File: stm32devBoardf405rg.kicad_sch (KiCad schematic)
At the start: 54 parts, among them J1 Screw_Terminal_01x02, J2 SWD, J3 Conn_01x04, J4 Conn_01x04, J5 USB_B_Micro, Q1 AO3401A, SW1 SW_SPDT, U1 STM32F405RGT6, U2 USBLC6-2SC6, Y1 16MZ

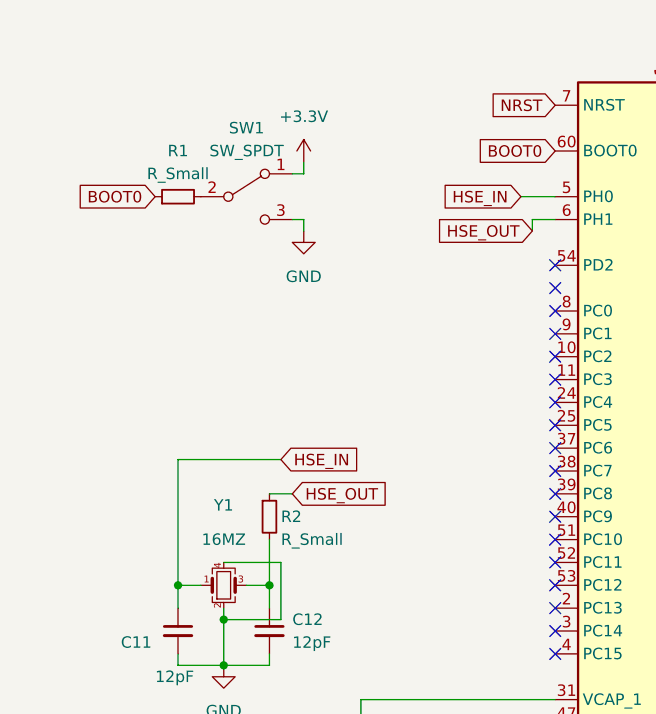
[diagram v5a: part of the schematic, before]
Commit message: added footprint II
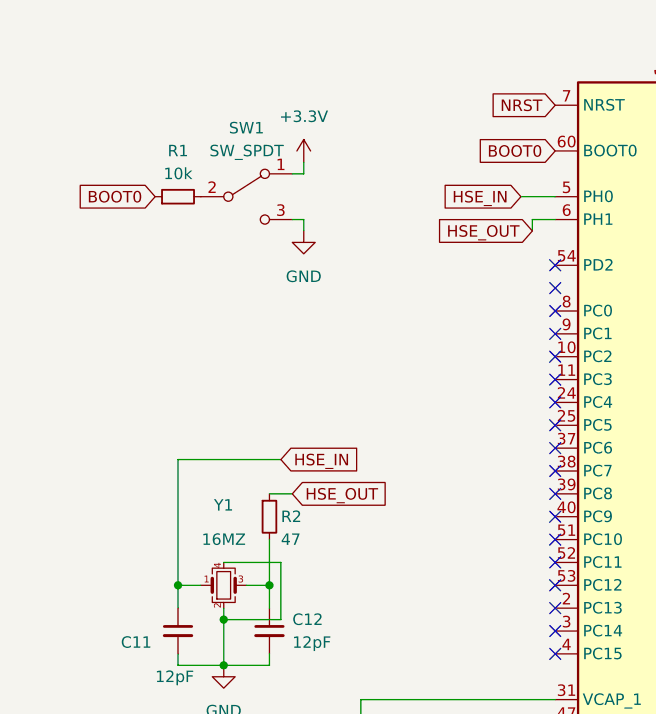
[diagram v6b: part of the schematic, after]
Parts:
- F1: footprint (none) -> Fuse:Fuse_1206_3216Metric
- FB1, L1, L2: footprint (none) -> Inductor_SMD:L_0805_2012Metric
- R1: value R_Small -> 10k; footprint (none) -> Resistor_SMD:R_0402_1005Metric
- R10, R11, R12, R13, R16, R3, R4, R5, R6, R7, R8, R9: footprint (none) -> Resistor_SMD:R_0603_1608Metric
- R14, R15: footprint (none) -> Resistor_SMD:R_0402_1005Metric
- R2: value R_Small -> 47; footprint (none) -> Resistor_SMD:R_0402_1005Metric
- SW1: footprint (none) -> Button_Switch_SMD:SW_SPDT_PCM12
- TPMP1: footprint (none) -> Package_TO_SOT_SMD:SOT-23-6
- Y1: footprint (none) -> Crystal:Crystal_SMD_3225-4Pin_3.2x2.5mm
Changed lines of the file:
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@@
       (effects (font (size 1.27 1.27)) (justify left))
     )
-    (property "Value" "R_Small" (at 43.18 337.82 0)
-      (effects (font (size 1.27 1.27)) (justify left))
-    )
-    (property "Footprint" "" (at 41.91 335.28 0)
+    (property "Value" "47" (at 43.18 337.82 0)
+      (effects (font (size 1.27 1.27)) (justify left))
+    )
+    (property "Footprint" "Resistor_SMD:R_0402_1005Metric" (at 41.91 335.28 0)
       (effects (font (size 1.27 1.27)) hide)
     )
@@
       (effects (font (size 1.27 1.27)))
     )
-    (property "Footprint" "" (at 130.81 144.78 0)
+    (property "Footprint" "Inductor_SMD:L_0805_2012Metric" (at 130.81 144.78 0)
       (effects (font (size 1.27 1.27)) hide)
     )
@@
       (effects (font (size 1.27 1.27)))
     )
-    (property "Footprint" "" (at 53.34 134.112 90)
+    (property "Footprint" "Inductor_SMD:L_0805_2012Metric" (at 53.34 134.112 90)
       (effects (font (size 1.27 1.27)) hide)
     )
@@
       (effects (font (size 1.27 1.27)) (justify left))
     )
-    (property "Footprint" "" (at 135.89 156.21 0)
+    (property "Footprint" "Resistor_SMD:R_0603_1608Metric" (at 135.89 156.21 0)
       (effects (font (size 1.27 1.27)) hide)
     )
@@
       (effects (font (size 1.27 1.27)) (justify left))
     )
-    (property "Footprint" "" (at 66.04 173.99 0)
+    (property "Footprint" "Resistor_SMD:R_0603_1608Metric" (at 66.04 173.99 0)
       (effects (font (size 1.27 1.27)) hide)
     )
@@
       (effects (font (size 1.27 1.27)) (justify left))
     )
-    (property "Footprint" "" (at 135.89 149.86 0)
+    (property "Footprint" "Resistor_SMD:R_0603_1608Metric" (at 135.89 149.86 0)
       (effects (font (size 1.27 1.27)) hide)
     )
@@
       (effects (font (size 1.27 1.27)))
     )
-    (property "Footprint" "" (at 274.32 270.51 0)
+    (property "Footprint" "Resistor_SMD:R_0603_1608Metric" (at 274.32 270.51 0)
       (effects (font (size 1.27 1.27)) hide)
     )
@@
       (effects (font (size 1.27 1.27)) (justify left))
     )
-    (property "Footprint" "" (at 149.86 356.87 0)
+    (property "Footprint" "Resistor_SMD:R_0402_1005Metric" (at 149.86 356.87 0)
       (effects (font (size 1.27 1.27)) hide)
     )
@@
       (effects (font (size 1.27 1.27)) (justify left))
     )
-    (property "Footprint" "" (at 135.89 161.29 0)
+    (property "Footprint" "Resistor_SMD:R_0603_1608Metric" (at 135.89 161.29 0)
       (effects (font (size 1.27 1.27)) hide)
     )
@@
       (effects (font (size 1.27 1.27)))
     )
-    (property "Footprint" "" (at 34.29 134.62 0)
+    (property "Footprint" "Fuse:Fuse_1206_3216Metric" (at 34.29 134.62 0)
       (effects (font (size 1.27 1.27)) (justify left) hide)
     )
@@
       (effects (font (size 1.27 1.27)))
     )
-    (property "Value" "R_Small" (at 31.75 297.18 90)
-      (effects (font (size 1.27 1.27)))
-    )
-    (property "Footprint" "" (at 31.75 299.72 0)
+    (property "Value" "10k" (at 31.75 297.18 90)
+      (effects (font (size 1.27 1.27)))
+    )
+    (property "Footprint" "Resistor_SMD:R_0402_1005Metric" (at 31.75 299.72 0)
       (effects (font (size 1.27 1.27)) hide)
     )
@@
       (effects (font (size 1.27 1.27)) (justify left))
     )
-    (property "Footprint" "" (at 135.89 168.91 0)
+    (property "Footprint" "Resistor_SMD:R_0603_1608Metric" (at 135.89 168.91 0)
       (effects (font (size 1.27 1.27)) hide)
     )
@@
       (effects (font (size 1.27 1.27)) (justify left))
     )
-    (property "Footprint" "" (at 139.7 356.87 0)
+    (property "Footprint" "Resistor_SMD:R_0402_1005Metric" (at 139.7 356.87 0)
       (effects (font (size 1.27 1.27)) hide)
     )
@@
       (effects (font (size 1.27 1.27)))
     )
-    (property "Footprint" "" (at 114.3 264.16 0)
+    (property "Footprint" "Inductor_SMD:L_0805_2012Metric" (at 114.3 264.16 0)
       (effects (font (size 1.27 1.27)) hide)
     )
@@
       (effects (font (size 1.27 1.27)))
     )
-    (property "Footprint" "" (at 39.37 299.72 0)
+    (property "Footprint" "Button_Switch_SMD:SW_SPDT_PCM12" (at 39.37 299.72 0)
       (effects (font (size 1.27 1.27)) hide)
     )
@@
       (effects (font (size 1.27 1.27)))
     )
-    (property "Footprint" "" (at 36.83 342.9 0)
+    (property "Footprint" "Crystal:Crystal_SMD_3225-4Pin_3.2x2.5mm" (at 36.83 342.9 0)
       (effects (font (size 1.27 1.27)) hide)
     )
@@
       (effects (font (size 1.27 1.27)))
     )
-    (property "Footprint" "" (at 274.32 278.13 0)
+    (property "Footprint" "Resistor_SMD:R_0603_1608Metric" (at 274.32 278.13 0)
       (effects (font (size 1.27 1.27)) hide)
     )
@@
       (effects (font (size 1.27 1.27)))
     )
-    (property "Footprint" "" (at 274.32 267.97 0)
+    (property "Footprint" "Resistor_SMD:R_0603_1608Metric" (at 274.32 267.97 0)
       (effects (font (size 1.27 1.27)) hide)
     )
@@
       (effects (font (size 1.27 1.27)) (justify left))
     )
-    (property "Footprint" "" (at 139.7 302.26 0)
+    (property "Footprint" "Resistor_SMD:R_0603_1608Metric" (at 139.7 302.26 0)
       (effects (font (size 1.27 1.27)) hide)
     )
@@
       (effects (font (size 1.27 1.27)))
     )
-    (property "Footprint" "" (at 90.17 142.24 0)
+    (property "Footprint" "Package_TO_SOT_SMD:SOT-23-6" (at 90.17 142.24 0)
       (effects (font (size 1.27 1.27)) hide)
     )
@@
       (effects (font (size 1.27 1.27)))
     )
-    (property "Footprint" "" (at 274.32 273.05 0)
+    (property "Footprint" "Resistor_SMD:R_0603_1608Metric" (at 274.32 273.05 0)
       (effects (font (size 1.27 1.27)) hide)
     )
@@
       (effects (font (size 1.27 1.27)) (justify left))
     )
-    (property "Footprint" "" (at 184.15 147.32 0)
+    (property "Footprint" "Resistor_SMD:R_0603_1608Metric" (at 184.15 147.32 0)
       (effects (font (size 1.27 1.27)) hide)
     )
@@
       (effects (font (size 1.27 1.27)) (justify left))
     )
-    (property "Footprint" "" (at 66.04 166.37 0)
-      (effects (font (size 1.27 1.27)) hide)
-    )
+    (property "Footprint" "Resistor_SMD:R_0603_1608Metric" (at 66.04 166.37 0)
+      (effects (font (size 1.27 1.27)) hide)
+    )

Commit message: added clearance for pcb
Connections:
- net BUCK_FB: now also C15.1, R7.1, R9.2
- no-connect marks 45 -> 43
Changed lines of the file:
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@@
   (no_connect (at 109.22 345.44))
   (no_connect (at 109.22 302.26))
-  (no_connect (at 73.66 309.88))
   (no_connect (at 109.22 292.1))
   (no_connect (at 271.78 275.59))
@@
   (no_connect (at 109.22 307.34))
   (no_connect (at 203.2 334.01))
-  (no_connect (at 109.22 330.2))
   (no_connect (at 73.66 347.98))
   (no_connect (at 73.66 332.74))
@@
     (stroke (width 0) (type default))
   )
+  (wire (pts (xy 132.08 165.1) (xy 135.89 165.1))
+    (stroke (width 0) (type default))
+  )
   (wire (pts (xy 86.36 269.24) (xy 91.44 269.24))
     (stroke (width 0) (type default))
@@
       (effects (font (size 1.27 1.27)) (justify right) hide)
     )
+  )
+  (global_label "BUCK_FB" (shape input) (at 132.08 165.1 180) (fields_autoplaced)
+    (effects (font (size 1.27 1.27)) (justify right))
+    (property "Intersheetrefs" "${INTERSHEET_REFS}" (at 120.6281 165.1 0)
+      (effects (font (size 1.27 1.27)) (justify right) hide)
+    )

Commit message: added pin no to TPMP2359 buck regulator
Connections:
- net BUCK_BS: now also TPMP1.1 (BS); no longer TPMP1. (SW)
- net BUCK_EN: now also TPMP1.4 (EN); no longer TPMP1. (SW)
- net BUCK_FB: now also TPMP1.3 (FB); no longer TPMP1. (SW)
- net BUCK_IN: now also TPMP1.5 (IN); no longer TPMP1. (SW)
- net BUCK_SW: now also TPMP1.6 (SW); no longer TPMP1. (SW)
- net GND: now also TPMP1.2 (GND); no longer TPMP1. (SW)
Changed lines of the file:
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@@
       (effects (font (size 1.27 1.27)))
     )
-    (property "Footprint" "Package_TO_SOT_SMD:SOT-23-6" (at 90.17 142.24 0)
+    (property "Footprint" "Package_TO_SOT_SMD:SOT-23-6" (at 97.79 158.75 0)
       (effects (font (size 1.27 1.27)) hide)
     )
@@
       (effects (font (size 1.27 1.27)) hide)
     )
-    (pin "")
-    (pin "")
-    (pin "")
-    (pin "")
-    (pin "")
-    (pin "")
+    (pin "1")
+    (pin "4")
+    (pin "3")
+    (pin "2")
+    (pin "5")
+    (pin "6")
     (instances
       (project "stm32devBoardf405rg"
